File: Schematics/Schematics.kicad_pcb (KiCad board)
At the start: 2 copper layers, 1 part, among them U1 ATmega328P-PU

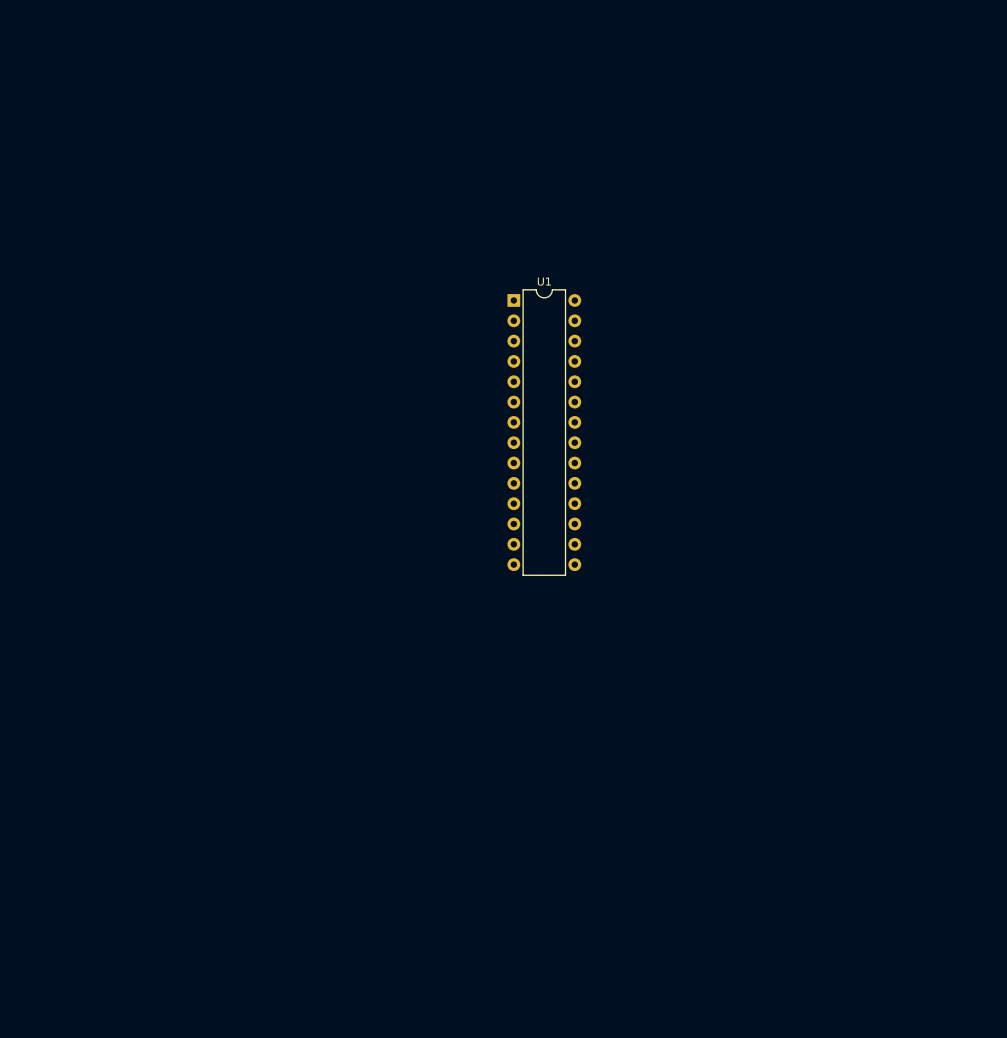
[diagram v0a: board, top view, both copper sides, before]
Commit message: The schematics were altered. A Circuit board layout was added.
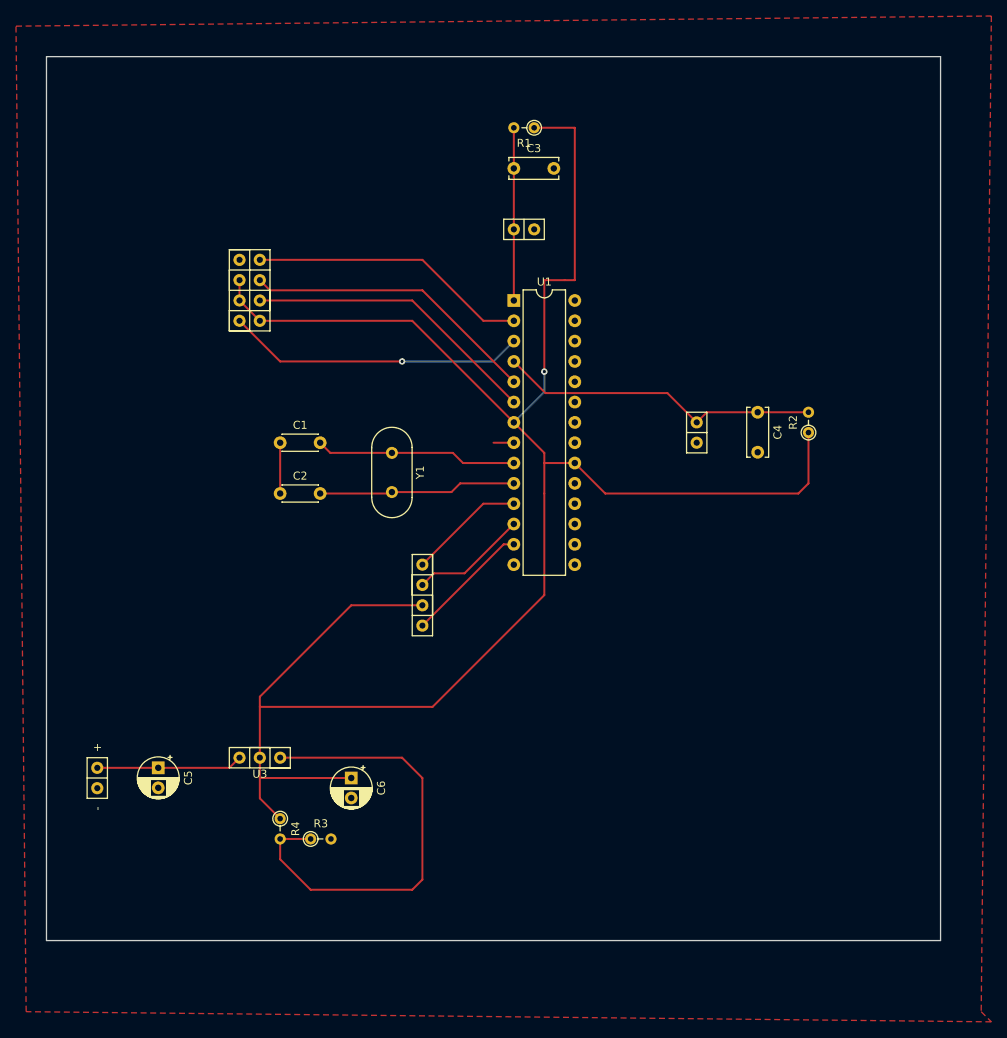
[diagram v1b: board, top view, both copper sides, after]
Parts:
- added BT1: Battery_Cell, Laundry_Pulse_Lib:Connector_Battery, F.Cu at (27.9, 113.0)
- added C1: 22pF, Capacitor_THT:C_Disc_D4.3mm_W1.9mm_P5.00mm, F.Cu at (50.8, 71.1)
- added C2: 22pF, Capacitor_THT:C_Disc_D4.3mm_W1.9mm_P5.00mm, F.Cu at (50.8, 77.5)
- added C3: 0.1uF, Capacitor_THT:C_Disc_D6.0mm_W2.5mm_P5.00mm, F.Cu at (80.0, 36.8)
- added C4: 0.1uF, Capacitor_THT:C_Disc_D6.0mm_W2.5mm_P5.00mm, F.Cu at (110.5, 67.3)
- added C5: 0.1uF, Capacitor_THT:CP_Radial_D5.0mm_P2.50mm, F.Cu at (35.6, 111.8)
- added C6: 0.1uF, Capacitor_THT:CP_Radial_D5.0mm_P2.50mm, F.Cu at (59.7, 113.0)
- added D1: LED_BGAR, Laundry_Pulse_Lib:Connector_LED, F.Cu at (68.6, 90.2)
- added R1: 10k, Resistor_THT:R_Axial_DIN0204_L3.6mm_D1.6mm_P2.54mm_Vertical, F.Cu at (82.5, 31.8)
- added R2: 10k, Resistor_THT:R_Axial_DIN0204_L3.6mm_D1.6mm_P2.54mm_Vertical, F.Cu at (116.8, 69.8)
- added R3: 390, Resistor_THT:R_Axial_DIN0204_L3.6mm_D1.6mm_P2.54mm_Vertical, F.Cu at (54.6, 120.7)
- added R4: 240, Resistor_THT:R_Axial_DIN0204_L3.6mm_D1.6mm_P2.54mm_Vertical, F.Cu at (50.8, 118.1)
- added SW1: SW_Push, Laundry_Pulse_Lib:Connector_Button, F.Cu at (81.3, 44.5)
- added SW2: SW_Push, Laundry_Pulse_Lib:Connector_Button, F.Cu at (102.9, 69.8)
- added U2: ESP-01, Laundry_Pulse_Lib:ESP01_Footprint, F.Cu at (47.0, 52.1)
- added U3: LM317, Laundry_Pulse_Lib:LM317_Custom, F.Cu at (48.3, 110.5)
- added Y1: Crystal, Crystal:Crystal_HC18-U_Vertical, F.Cu at (64.8, 72.4)
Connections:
- U1 pad 14: Net-(U1-Pad14) -> (no net)
- U1 pad 15: Net-(U1-Pad15) -> (no net)
- U1 pad 16: Net-(U1-Pad16) -> (no net)
- U1 pad 17: Net-(U1-Pad17) -> (no net)
- U1 pad 18: Net-(U1-Pad18) -> (no net)
- U1 pad 19: Net-(U1-Pad19) -> (no net)
- U1 pad 21: Net-(U1-Pad21) -> (no net)
- U1 pad 23: Net-(U1-Pad23) -> (no net)
- U1 pad 24: Net-(U1-Pad24) -> (no net)
- U1 pad 25: Net-(U1-Pad25) -> (no net)
- U1 pad 26: Net-(U1-Pad26) -> (no net)
- U1 pad 27: Net-(U1-Pad27) -> (no net)
- U1 pad 28: Net-(U1-Pad28) -> (no net)
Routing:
- net +3V3: track 0.00 -> 249.2 mm, vias 0 -> 1
- net Net-(R3-Pad1): track 0.00 -> 57.8 mm
- net /INT0: track 0.00 -> 40.5 mm
- net /TX: track 0.00 -> 37.4 mm, vias 0 -> 1
- net /REST: track 0.00 -> 37.0 mm
- net /CH_PD: track 0.00 -> 37.0 mm
- net /RX: track 0.00 -> 34.9 mm
- net Net-(C1-Pad2): track 0.00 -> 25.3 mm
- net Net-(C2-Pad2): track 0.00 -> 24.7 mm
- net Net-(C3-Pad1): track 0.00 -> 21.6 mm
- net Net-(BT1-Pad1): track 0.00 -> 18.3 mm
- net Net-(D1-Pad4): track 0.00 -> 15.6 mm
- net Net-(D1-Pad2): track 0.00 -> 14.6 mm
- net Net-(D1-Pad1): track 0.00 -> 14.6 mm
- net GND: track 0.00 -> 8.89 mm
- added copper zone on F.Cu, net GND
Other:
- board outline added: 111.8 x 110.5 mm
